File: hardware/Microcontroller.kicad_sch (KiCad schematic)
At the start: 95 parts, among them J10 UART, J2 USB_C, J3 OLED, J8 +12V, J9 STLink, Q4 IRLML2244, Q5 MMBT3904, SW1 Button Up, SW2 Button Down, SW3 Reset, SW4 Button Escape, SW5 Button Left, SW6 Button Enter, SW7 Button Right, SW8 Button Power, U10 STM32F405RGTx, U11 TPS7A2033, U2 TP6841S6, U3 USBLC6-2, X1 12 MHz TCXO, Y1 8 MHz

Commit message: Updated schematic title block
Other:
- company: (none) -> M17Project
- title: (none) -> Module17
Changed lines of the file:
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@@
 (kicad_sch (version 20230121) (generator eeschema)
   (paper "A4")
+  (title_block
+    (title "Module17")
+    (date "2023-07-18")
+    (rev "Rev 1.0")
+    (company "M17Project")
+    (comment 1 "Mathis - DB9MAT")
+    (comment 2 "Wojciech - SP5WWP")
+    (comment 3 "Authors:")
+  )
   (junction (at 35.56 74.93) (diameter 1.016) (color 0 0 0 0)
   )

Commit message: Updated D8, D9 MPN to generic MPN
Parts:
- D8, D9: MPN BAT60AE6327HTSA1 -> Generic Schottky/10Vr/2A/SOD323-2
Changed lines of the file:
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@@
       (effects (font (size 1.27 1.27)) hide)
     )
-    (property "MPN" "BAT60AE6327HTSA1" (at 219.71 22.86 0)
+    (property "MPN" "Generic Schottky/10Vr/2A/SOD323-2" (at 219.71 22.86 0)
       (effects (font (size 1.27 1.27)) hide)
     )
@@
       (effects (font (size 1.27 1.27)) hide)
     )
-    (property "MPN" "BAT60AE6327HTSA1" (at 189.23 147.32 0)
-      (effects (font (size 1.27 1.27)) hide)
-    )
+    (property "MPN" "Generic Schottky/10Vr/2A/SOD323-2" (at 189.23 147.32 0)
+      (effects (font (size 1.27 1.27)) hide)
+    )

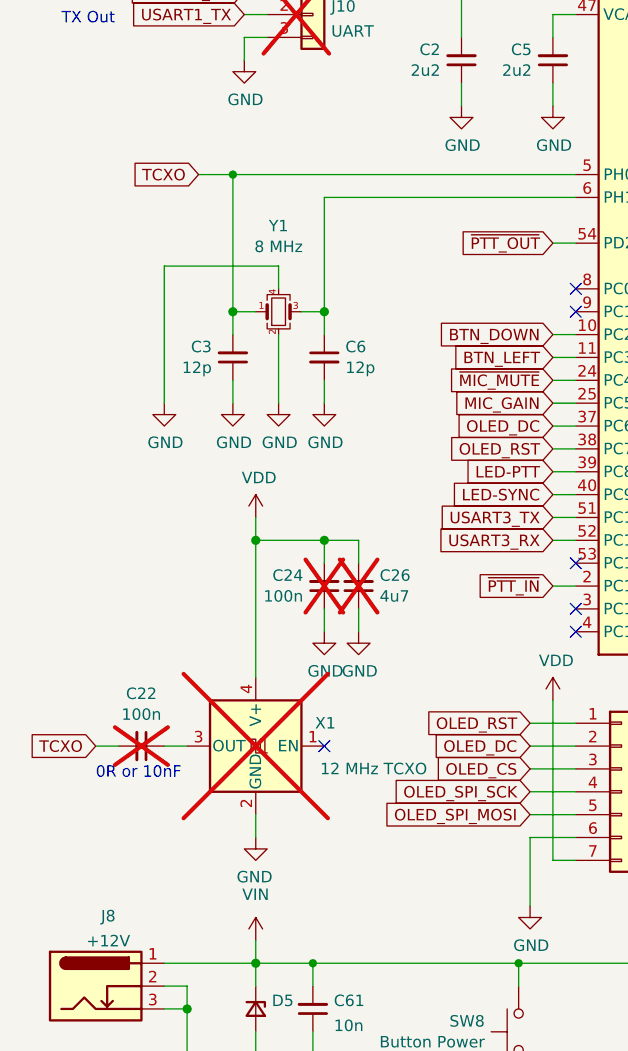
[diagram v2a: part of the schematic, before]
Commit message: Removed unused TCXO
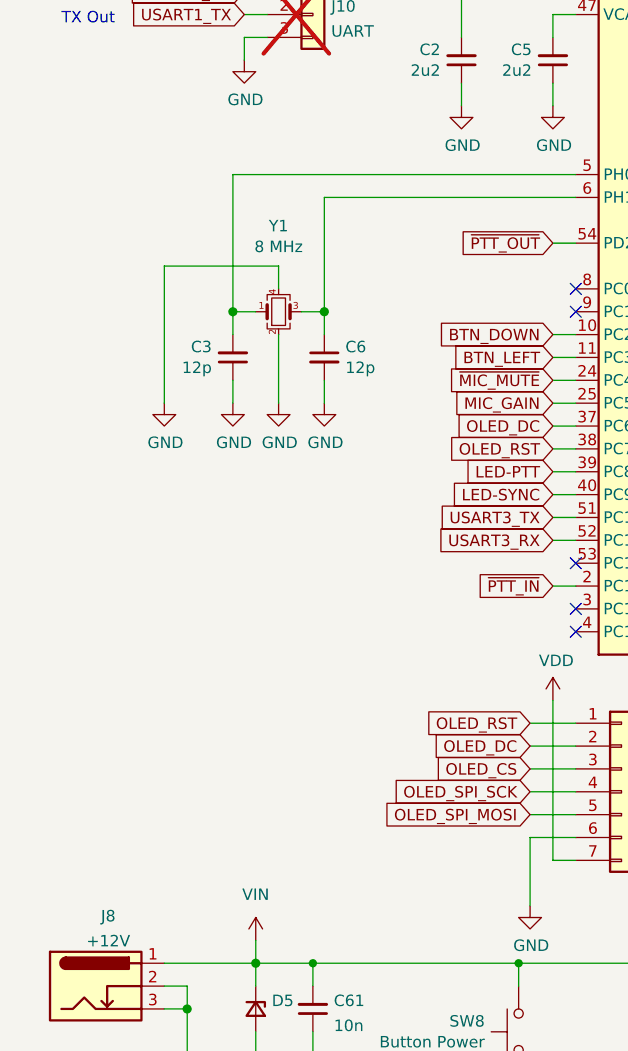
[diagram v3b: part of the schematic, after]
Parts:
- removed C22, C24: 100n, pkl_dipol:C_0603, symbol pkl_device:pkl_C_Small
- removed C26: 4u7, pkl_dipol:C_0603, symbol pkl_device:pkl_C_Small
- removed X1: 12 MHz TCXO, Oscillator:Oscillator_SMD_Abracon_ASE-4Pin_3.2x2.5mm, symbol Oscillator:XO32
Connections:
- net TCXO: no longer names the net of C3.2, U10.5 (PH0), Y1.1
- no-connect marks 12 -> 11
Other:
- note removed: "0R or 10nF"

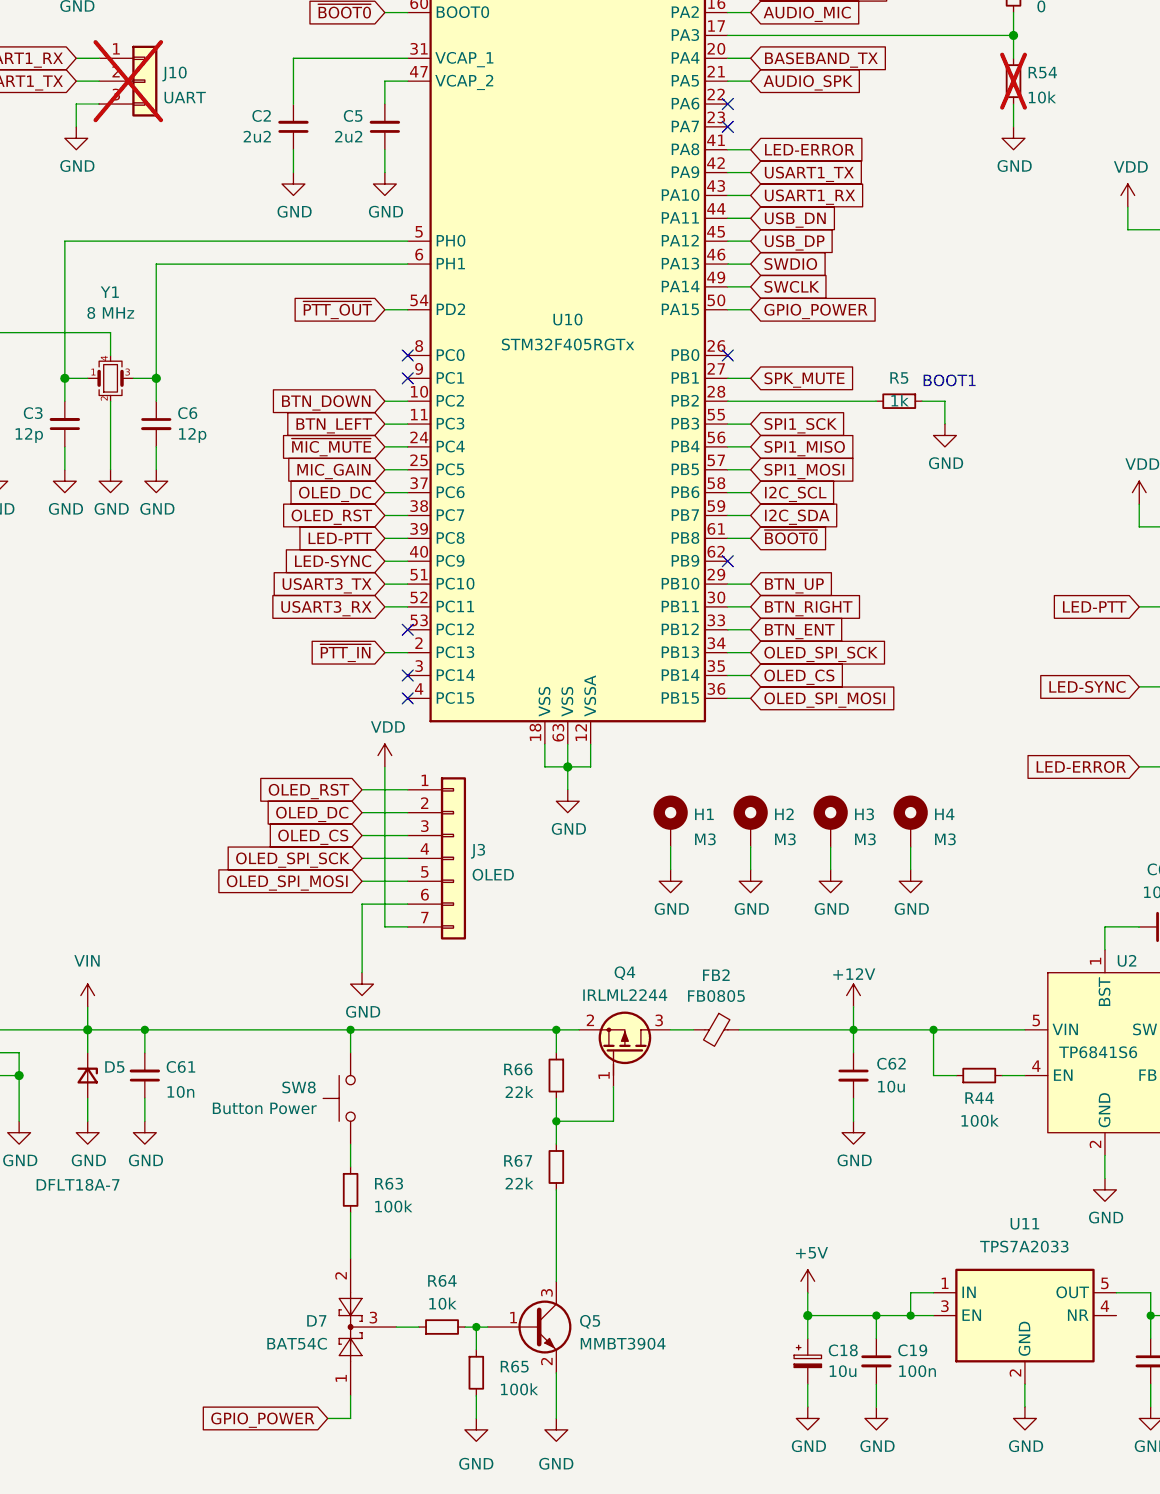
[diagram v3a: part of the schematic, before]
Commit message: Added 10k pull-down
Solves the no-self-shutdown issue
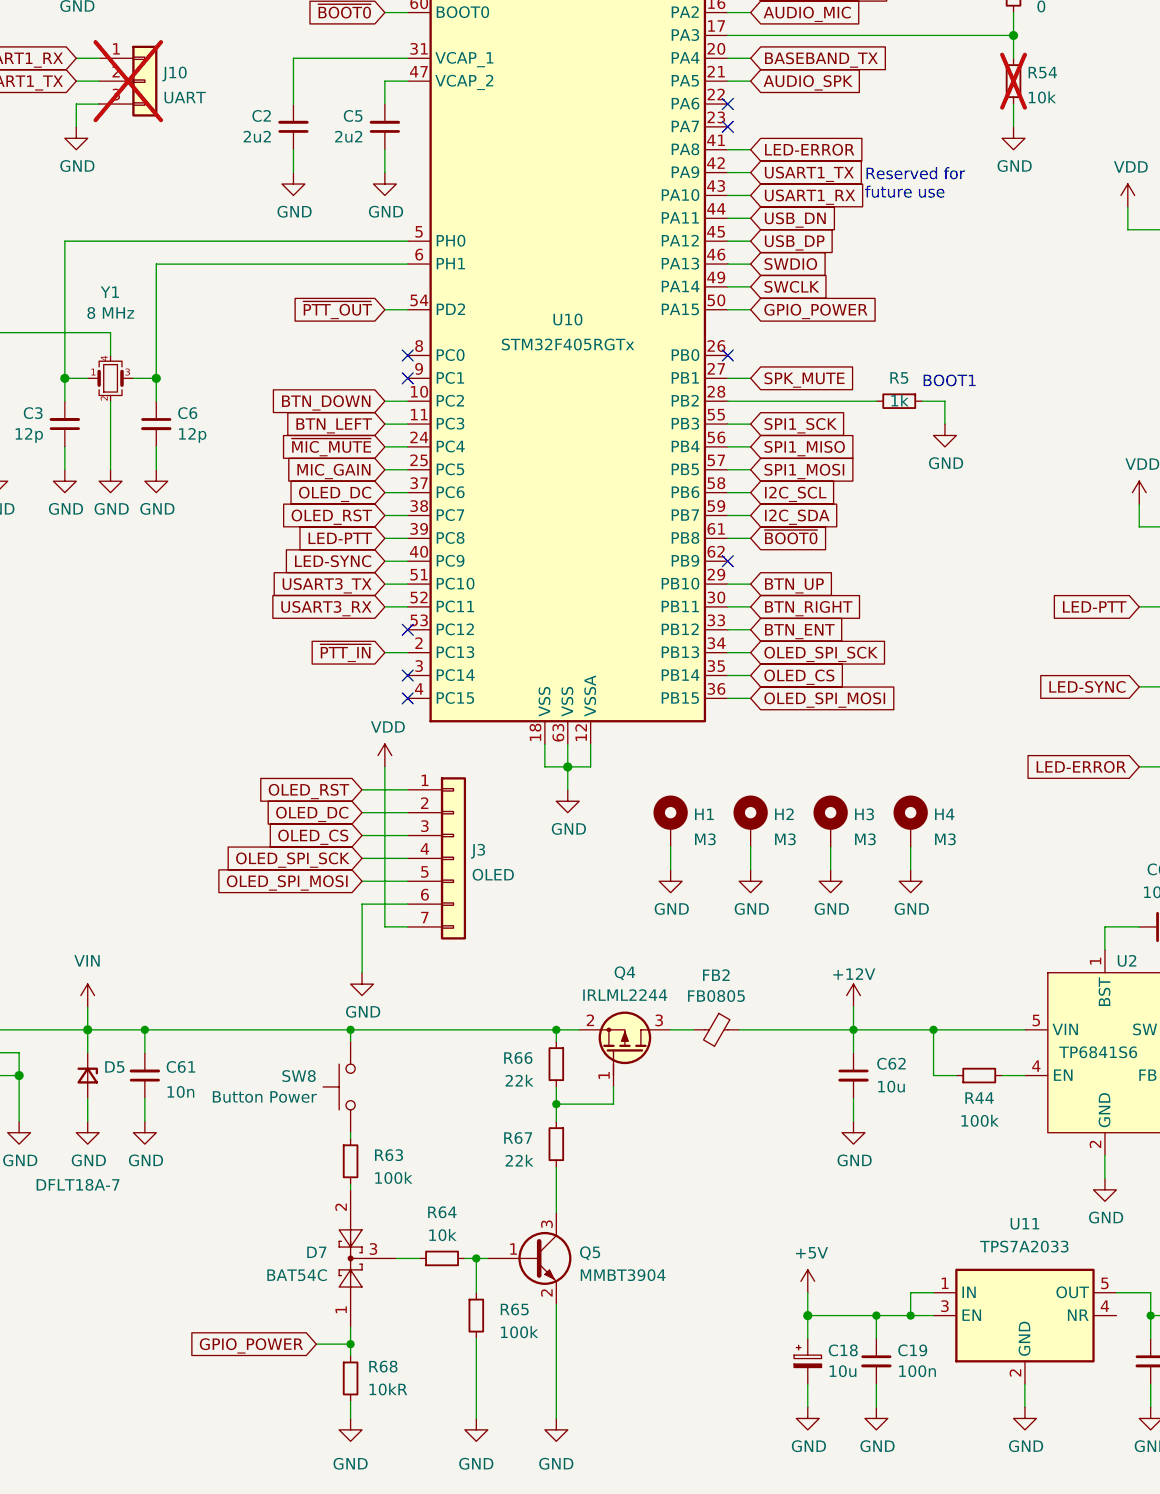
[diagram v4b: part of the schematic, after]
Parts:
- added R68: 10kR, pkl_dipol:R_0603, symbol Device:R_Small
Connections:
- net GND: now also R68.2
- net GPIO_POWER: now also R68.1
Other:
- note added: "Reserved for future use"
- moved on the sheet: D7, Q5, R63, R64, R65, R66, R67, SW8

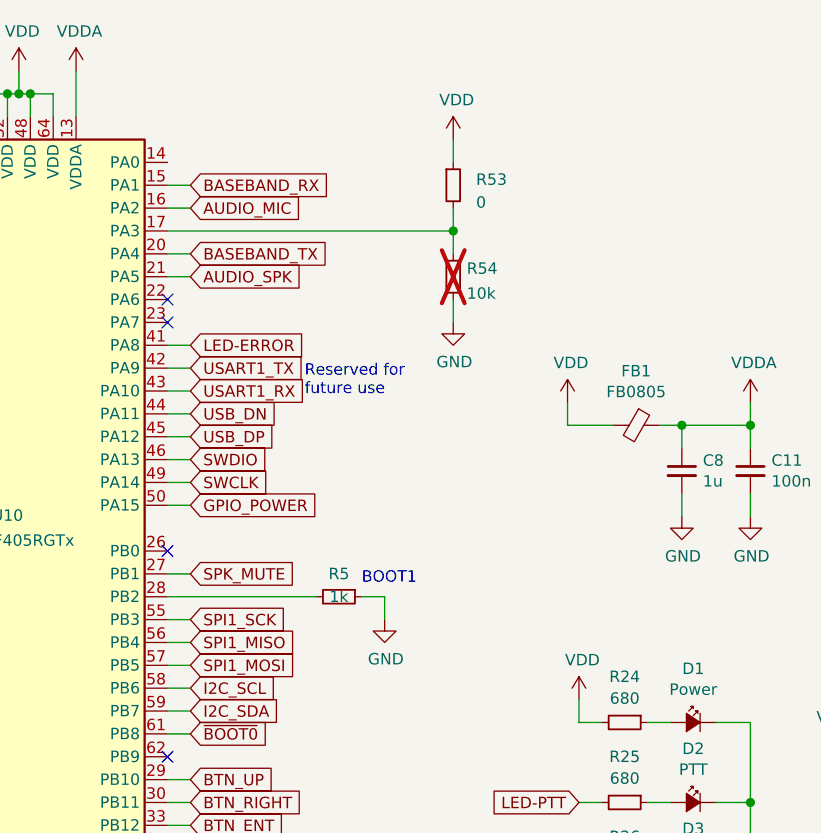
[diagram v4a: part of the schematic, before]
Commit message: Set the revision detection pins to the correct voltages for Rev 1.0
PA3 set to VDD/2. PB0 set to GND.
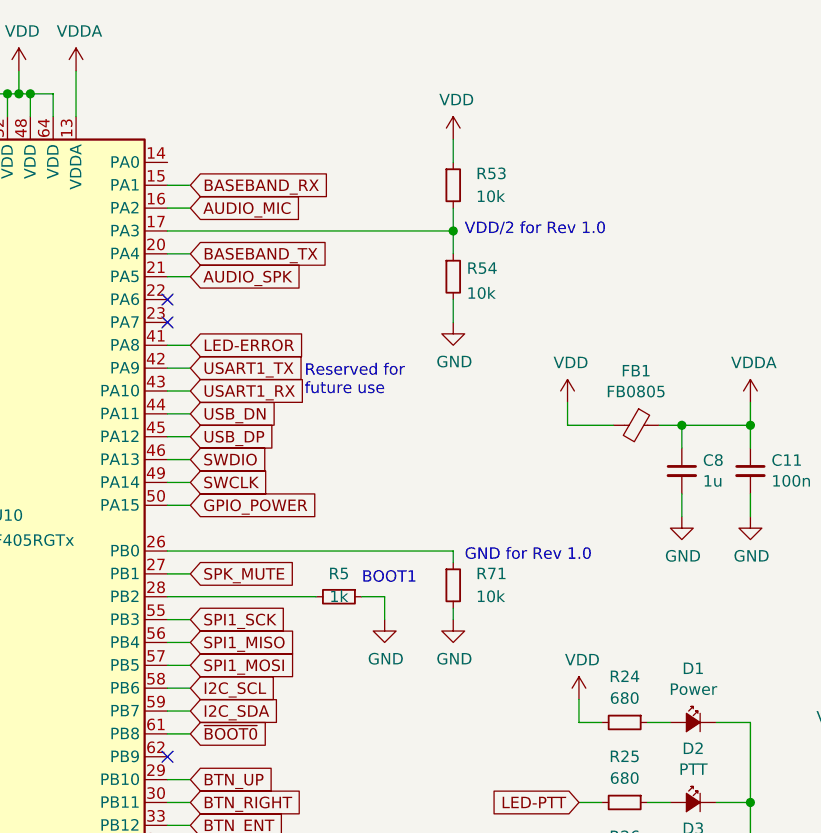
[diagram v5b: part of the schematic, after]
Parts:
- added R71: 10k, pkl_dipol:R_0603, symbol pkl_device:pkl_R_Small
- R53: value 0 -> 10k; MPN Generic R/2k7/0603 -> Generic R/10k/0603
- R54: now fitted
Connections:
- net GND: now also R71.2
- net at U10.26 (PB0): now also R71.1
- no-connect marks 11 -> 10
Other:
- note added: "GND for Rev 1.0"
- note added: "VDD/2 for Rev 1.0"
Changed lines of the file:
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@@
   (no_connect (at 73.66 110.49))
   (no_connect (at 109.22 46.99))
-  (no_connect (at 109.22 72.39))
   (no_connect (at 73.66 72.39))
   (no_connect (at 73.66 107.95))
@@
     (stroke (width 0) (type solid))
   )
+  (wire (pts (xy 140.97 78.74) (xy 140.97 80.01))
+    (stroke (width 0) (type default))
+  )
   (wire (pts (xy 247.65 110.49) (xy 247.65 113.03))
     (stroke (width 0) (type solid))
@@
     (stroke (width 0) (type solid))
   )
+  (wire (pts (xy 140.97 72.39) (xy 140.97 73.66))
+    (stroke (width 0) (type default))
+  )
   (wire (pts (xy 157.48 91.44) (xy 154.94 91.44))
     (stroke (width 0) (type solid))
@@
     (stroke (width 0) (type solid))
   )
+  (wire (pts (xy 109.22 72.39) (xy 140.97 72.39))
+    (stroke (width 0) (type default))
+  )
   (wire (pts (xy 208.28 148.59) (xy 208.28 151.13))
     (stroke (width 0) (type solid))
@@
     (effects (font (size 1.27 1.27)) (justify left bottom))
   )
+  (text "VDD/2 for Rev 1.0" (at 142.24 37.465 0)
+    (effects (font (size 1.27 1.27)) (justify left bottom))
+  )
   (text "RX In" (at 17.78 40.64 0)
     (effects (font (size 1.27 1.27)) (justify left bottom))
   )
+  (text "GND for Rev 1.0" (at 142.24 73.66 0)
+    (effects (font (size 1.27 1.27)) (justify left bottom))
+  )
   (label "xUDN" (at 217.17 38.1 0) (fields_autoplaced)
     (effects (font (size 1.27 1.27)) (justify left bottom))
@@
     )
   )
+  (symbol (lib_id "power:GND") (at 140.97 80.01 0) (unit 1)
+    (in_bom yes) (on_board yes) (dnp no)
+    (property "Reference" "#PWR0302" (at 140.97 86.36 0)
+      (effects (font (size 1.27 1.27)) hide)
+    )
+    (property "Value" "GND" (at 141.097 84.4042 0)
+      (effects (font (size 1.27 1.27)))
+    )
+    (property "Footprint" "" (at 140.97 80.01 0)
+      (effects (font (size 1.27 1.27)) hide)
+    )
+    (property "Datasheet" "" (at 140.97 80.01 0)
+      (effects (font (size 1.27 1.27)) hide)
+    )
+    (pin "1")
+    (instances
+      (project "M17-SmartMic"
+        (path "/59592280-3207-432b-a891-cd517ec5cf12/00000000-0000-0000-0000-0000612c95ef"
+          (reference "#PWR0302") (unit 1)
+        )
+      )
+    )
+  )
   (symbol (lib_id "power:GND") (at 38.1 157.48 0) (unit 1)
     (in_bom yes) (on_board yes) (dnp no)
@@
   (symbol (lib_id "pkl_device:pkl_R_Small") (at 140.97 31.75 0) (unit 1)
     (in_bom yes) (on_board yes) (dnp no) (fields_autoplaced)
-    (property "Reference" "R53" (at 143.51 31.115 0)
+    (property "Reference" "R53" (at 143.51 30.48 0)
       (effects (font (size 1.27 1.27)) (justify left))
     )
-    (property "Value" "0" (at 143.51 33.655 0)
+    (property "Value" "10k" (at 143.51 33.02 0)
       (effects (font (size 1.27 1.27)) (justify left))
     )
@@
       (effects (font (size 1.524 1.524)))
     )
-    (property "MPN" "Generic R/2k7/0603" (at 140.97 31.75 0)
+    (property "MPN" "Generic R/10k/0603" (at 140.97 31.75 0)
       (effects (font (size 1.27 1.27)) hide)
     )
@@
     )
   )
+  (symbol (lib_id "pkl_device:pkl_R_Small") (at 140.97 76.2 0) (unit 1)
+    (in_bom yes) (on_board yes) (dnp no) (fields_autoplaced)
+    (property "Reference" "R71" (at 143.51 74.93 0)
+      (effects (font (size 1.27 1.27)) (justify left))
+    )
+    (property "Value" "10k" (at 143.51 77.47 0)
+      (effects (font (size 1.27 1.27)) (justify left))
+    )
+    (property "Footprint" "pkl_dipol:R_0603" (at 140.97 76.2 0)
+      (effects (font (size 1.524 1.524)) hide)
+    )
+    (property "Datasheet" "" (at 140.97 76.2 0)
+      (effects (font (size 1.524 1.524)))
+    )
+    (property "MPN" "Generic R/10k/0603" (at 140.97 76.2 0)
+      (effects (font (size 1.27 1.27)) hide)
+    )
+    (pin "1")
+    (pin "2")
+    (instances
+      (project "M17-SmartMic"
+        (path "/59592280-3207-432b-a891-cd517ec5cf12/00000000-0000-0000-0000-0000612c95ef"
+          (reference "R71") (unit 1)
+        )
+      )
+    )
+  )
   (symbol (lib_id "Transistor_BJT:MMBT3904") (at 87.63 172.72 0) (unit 1)
     (in_bom yes) (on_board yes) (dnp no) (fields_autoplaced)
@@
   )
   (symbol (lib_id "pkl_device:pkl_R_Small") (at 140.97 41.91 0) (unit 1)
-    (in_bom yes) (on_board yes) (dnp yes) (fields_autoplaced)
+    (in_bom yes) (on_board yes) (dnp no) (fields_autoplaced)
     (property "Reference" "R54" (at 142.4687 41.0015 0)
       (effects (font (size 1.27 1.27)) (justify left))
